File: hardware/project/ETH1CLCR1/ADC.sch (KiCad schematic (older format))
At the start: 89 parts, among them Q1101 BC847W, Q1102 BC847W, Q1103 BC847W, Q1104 BC847W, U1101 ADG419BR, U1102 ADG419BR, U1103 REF192, U1104 AD8606-2-MSOP, U1105 AD8606-2-MSOP, U1106 AD7380, U1107 AD8605, U1108 LT6350, U1109 LT6350, U1110 OPA602, U1111 OPA602, U1112 PGA103, U1113 PGA103

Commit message: PCB layout
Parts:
- U1106: symbol ETH1CLCR1:AD7380 -> ETH1CLCR1-rescue:AD7380-ETH1CLCR1
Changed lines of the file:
@@
 Connection ~ 3850 6900
 $Comp
-L ETH1CLCR1:AD7380 U1106
+L ETH1CLCR1-rescue:AD7380-ETH1CLCR1 U1106
 U 1 1 5E5D364C
 P 3450 3650
+AR Path="/5E5D364C" Ref="U1106"  Part="1"
+AR Path="/5E402F62/5E5D364C" Ref="U1106"  Part="1"
 F 0 "U1106" H 3850 4400 50  0000 C CNN
 F 1 "AD7380" H 3850 4300 50  0000 C CNN

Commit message: PCB layout
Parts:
- added C1115, C1117, C1119, C1123, C1125, C1127, C1129, C1131: 100n, Capacitor_SMD:C_0603_1608Metric_Pad1.05x0.95mm_HandSolder, symbol Device:C
- renumbered C1115 to C1116, C1116 to C1118, C1117 to C1120, C1118 to C1121, C1119 to C1122, C1120 to C1124, C1121 to C1126, C1122 to C1128, C1123 to C1130, C1124 to C1132, C1125 to C1133, C1126 to C1134, C1127 to C1135, C1128 to C1136, C1129 to C1137, C1130 to C1138, R1141 to R1139, R1142 to R1140, R1139 to R1141, R1140 to R1142
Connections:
- net +15VF: now also C1115.1, C1119.1, C1125.1, C1129.1
- net -15VF: now also C1117.1, C1123.1, C1127.1, C1131.1
- net AGNDF: now also C1115.2, C1117.2, C1119.2, C1123.2, C1125.2, C1127.2, C1129.2, C1131.2

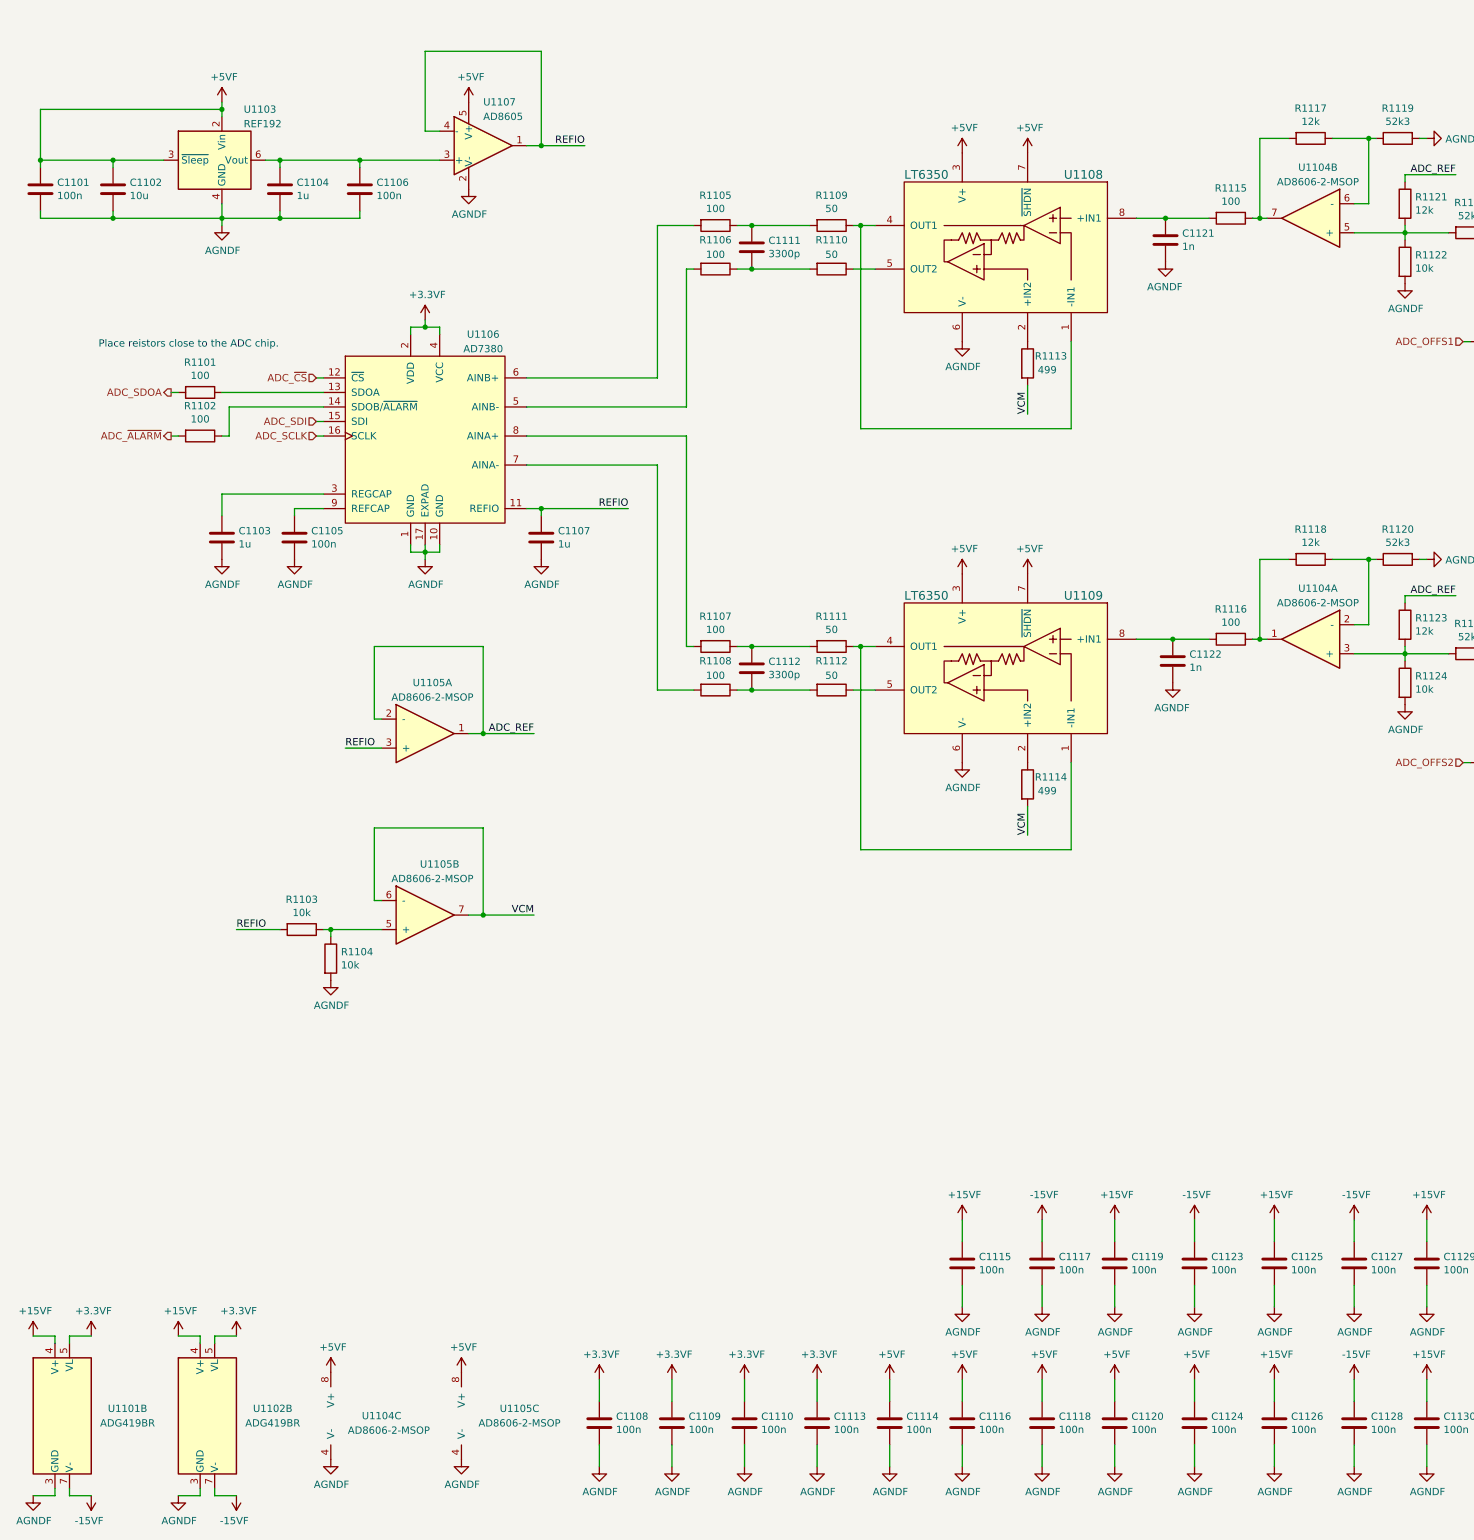
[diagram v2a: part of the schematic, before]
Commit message: Changed op-amps in ADC schematic.
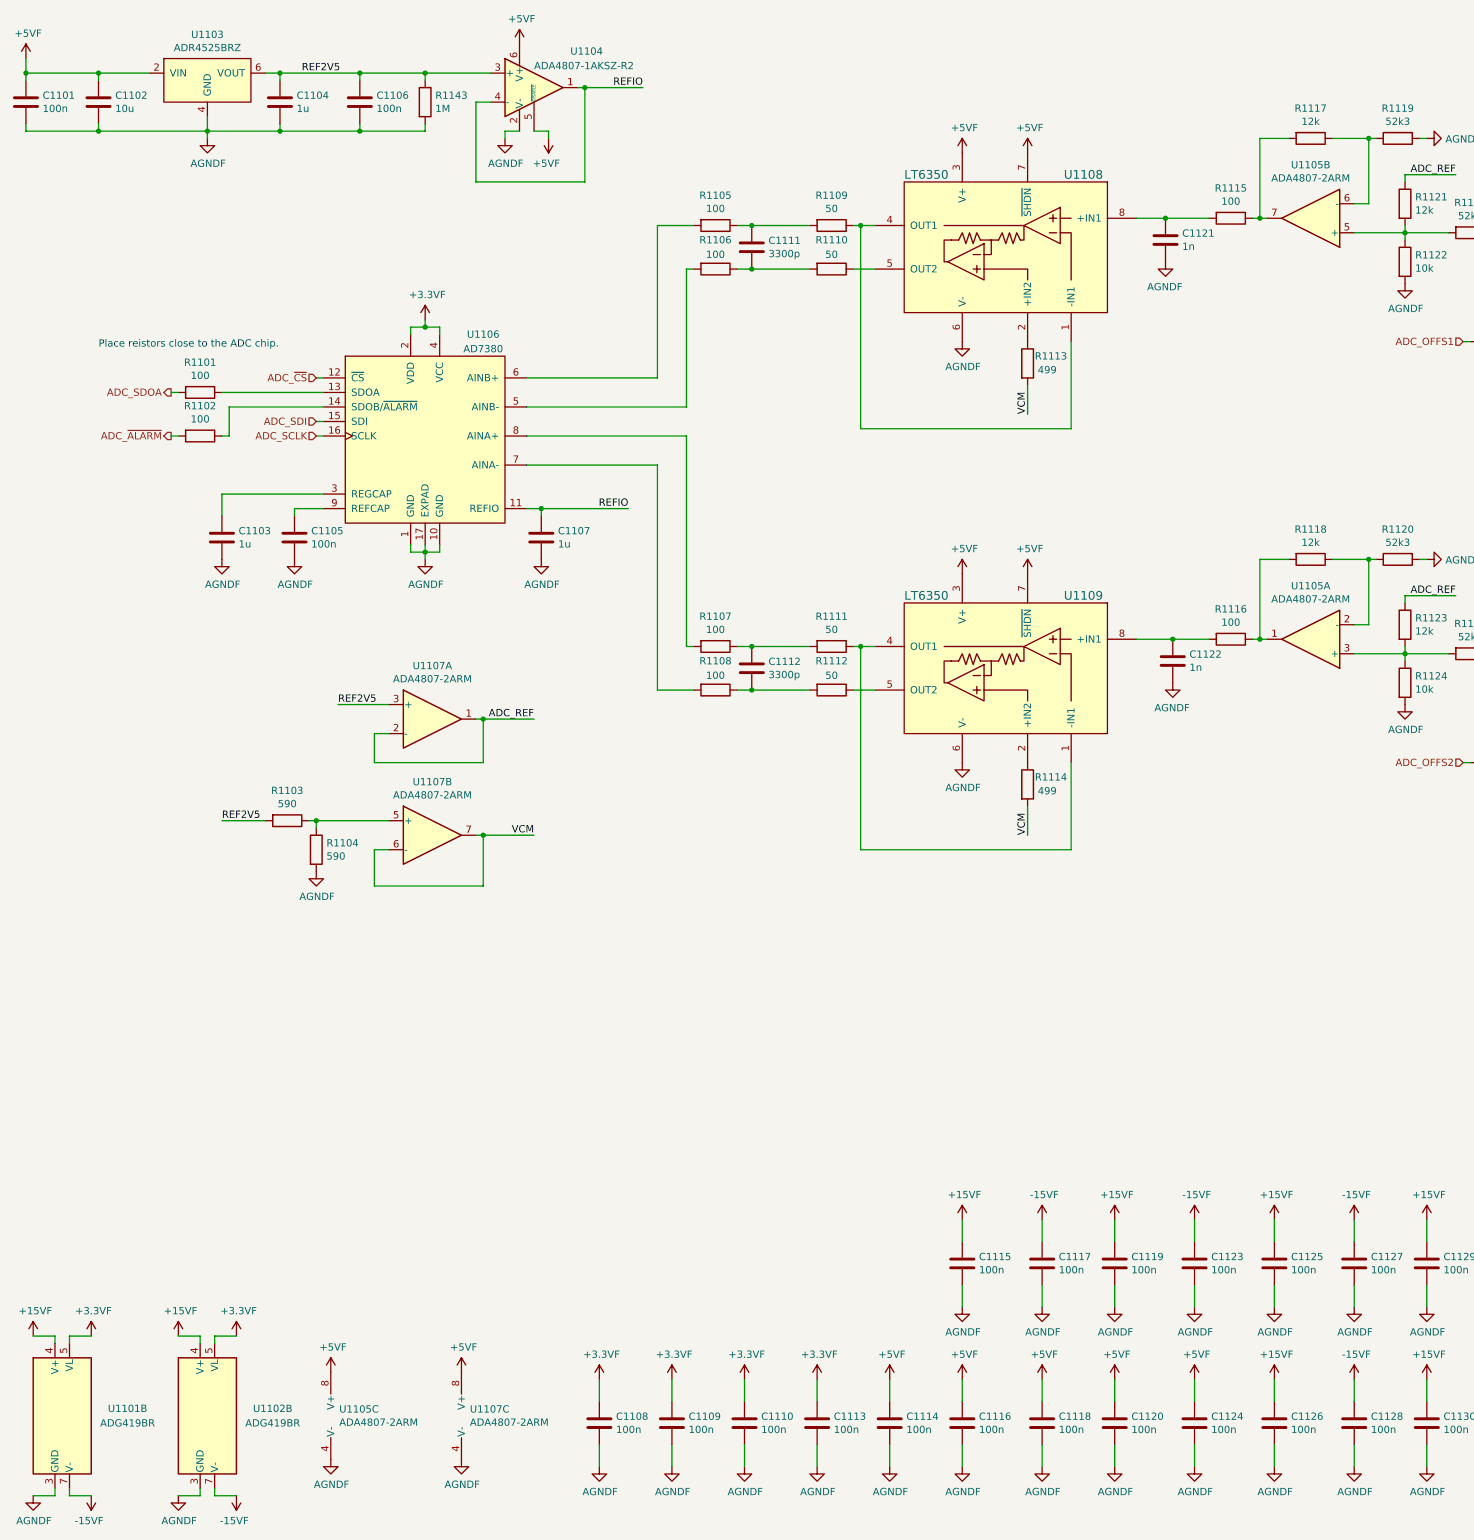
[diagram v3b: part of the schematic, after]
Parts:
- removed U1103: REF192, Package_SO:SSOP-8_3.9x5.05mm_P1.27mm, symbol Reference_Voltage:REF192
- removed U1104, U1105: AD8606-2-MSOP, Package_SO:MSOP-8_3x3mm_P0.65mm, symbol ETH1CLCR1:AD8606-2-MSOP
- removed U1107: AD8605, Package_TO_SOT_SMD:SOT-23-5_HandSoldering, symbol ETH1CLCR1:AD8605
- added R1143: 1M, Resistor_SMD:R_0603_1608Metric_Pad1.05x0.95mm_HandSolder, symbol Device:R
- added U1103: ADR4525BRZ, Package_SO:SOIC-8_3.9x4.9mm_P1.27mm, symbol ETH1CLCR1:ADR4525BRZ
- added U1104: ADA4807-1AKSZ-R2, Package_TO_SOT_SMD:SOT-363_SC-70-6_Handsoldering, symbol Amplifier_Operational:ADA4807-1
- added U1105, U1107: ADA4807-2ARM, Package_SO:MSOP-8_3x3mm_P0.65mm, symbol Amplifier_Operational:ADA4807-2ARM
- R1103, R1104: value 10k -> 590
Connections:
- net +5VF: now also U1103.2 (VIN), U1104.5 (~DISABLE), U1104.6 (V+), U1105.8 (V+), U1107.8 (V+)
- net ADC_REF: now also U1107.1, U1107.2 (-)
- net AGNDF: now also R1143.2, U1103.4 (GND), U1104.2 (V-), U1105.4 (V-), U1107.4 (V-)
- net REFIO: now also U1104.1, U1104.4 (-); no longer R1103.2
- net VCM: now also U1107.6 (-), U1107.7
- net at R1115.1, R1117.2: now also U1105.7
- net at R1103.1, R1104.1: now also U1107.5 (+)
- net at R1121.2, R1122.1, R1125.2: now also U1105.5 (+)
- net at R1117.1, R1119.1: now also U1105.6 (-)
- net at R1116.1, R1118.2: now also U1105.1
- net at R1123.2, R1124.1, R1126.2: now also U1105.3 (+)
- net at R1118.1, R1120.1: now also U1105.2 (-)
- net REF2V5: now reaches C1104.1, C1106.1
- net REF2V5: now also R1103.2, R1143.1, U1103.6 (VOUT), U1104.3 (+), U1107.3 (+)
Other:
- moved on the sheet: C1101, C1102, C1104, C1106, R1103, R1104

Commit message: PCB layout
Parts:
- added C1139, C1140: 100n, Capacitor_SMD:C_0603_1608Metric_Pad1.05x0.95mm_HandSolder, symbol Device:C
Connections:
- net AGNDF: now also C1139.2, C1140.2
- net at R1113.1, U1108.2 (+IN2): now also C1139.1
- net at R1114.1, U1109.2 (+IN2): now also C1140.1
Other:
- moved on the sheet: R1113, R1114
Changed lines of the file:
@@
 	1    0    0    -1
 $EndComp
-Text Label 7600 3450 1    50   ~ 0
+Text Label 7600 3800 1    50   ~ 0
 VCM
 Wire Wire Line
-	7600 3450 7600 3250
-Wire Wire Line
-	6450 5050 6550 5050
-Wire Wire Line
-	7900 2950 7900 3550
-Wire Wire Line
-	7900 3550 6450 3550
-Wire Wire Line
-	6450 3550 6450 2150
+	7600 3800 7600 3600
+Wire Wire Line
+	7900 2950 7900 3900
+Wire Wire Line
+	7900 3900 6450 3900
+Wire Wire Line
+	6450 3900 6450 2150
 Wire Wire Line
 	6550 2150 6450 2150
@@
 	6400 5350 6550 5350
 Wire Wire Line
-	6450 5050 6400 5050
-Wire Wire Line
 	6100 5050 5700 5050
 Wire Wire Line
@@
 	5600 5350 5700 5350
 Connection ~ 5700 5350
-Connection ~ 6450 5050
 Wire Wire Line
 	5300 5050 5250 5050
@@
 L Device:R R1113
 U 1 1 5E246E09
-P 7600 3100
-F 0 "R1113" H 7650 3150 50  0000 L CNN
-F 1 "499" H 7670 3055 50  0000 L CNN
-F 2 "Resistor_SMD:R_0603_1608Metric_Pad1.05x0.95mm_HandSolder" V 7530 3100 50  0001 C CNN
-F 3 "~" H 7600 3100 50  0001 C CNN
-	1    7600 3100
-	1    0    0    -1
-$EndComp
-Wire Wire Line
-	7900 5850 7900 6450
-Wire Wire Line
-	7900 6450 6450 6450
-Wire Wire Line
-	6450 5050 6450 6450
-Text Label 7600 6350 1    50   ~ 0
+P 7600 3450
+F 0 "R1113" H 7650 3500 50  0000 L CNN
+F 1 "499" H 7670 3405 50  0000 L CNN
+F 2 "Resistor_SMD:R_0603_1608Metric_Pad1.05x0.95mm_HandSolder" V 7530 3450 50  0001 C CNN
+F 3 "~" H 7600 3450 50  0001 C CNN
+	1    7600 3450
+	1    0    0    -1
+$EndComp
+Text Label 7600 6700 1    50   ~ 0
 VCM
 Wire Wire Line
-	7600 6350 7600 6150
+	7600 6700 7600 6500
 $Comp
 L Device:R R1114
 U 1 1 5E310DDA
-P 7600 6000
-F 0 "R1114" H 7650 6050 50  0000 L CNN
-F 1 "499" H 7670 5955 50  0000 L CNN
-F 2 "Resistor_SMD:R_0603_1608Metric_Pad1.05x0.95mm_HandSolder" V 7530 6000 50  0001 C CNN
-F 3 "~" H 7600 6000 50  0001 C CNN
-	1    7600 6000
+P 7600 6350
+F 0 "R1114" H 7650 6400 50  0000 L CNN
+F 1 "499" H 7670 6305 50  0000 L CNN
+F 2 "Resistor_SMD:R_0603_1608Metric_Pad1.05x0.95mm_HandSolder" V 7530 6350 50  0001 C CNN
+F 3 "~" H 7600 6350 50  0001 C CNN
+	1    7600 6350
 	1    0    0    -1
 $EndComp
@@
 	1    0    0    -1
 $EndComp
+$Comp
+L Device:C C1139
+U 1 1 5E3B70FC
+P 7200 3450
+F 0 "C1139" H 7315 3496 50  0000 L CNN
+F 1 "100n" H 7315 3405 50  0000 L CNN
+F 2 "Capacitor_SMD:C_0603_1608Metric_Pad1.05x0.95mm_HandSolder" H 7238 3300 50  0001 C CNN
+F 3 "~" H 7200 3450 50  0001 C CNN
+	1    7200 3450
+	1    0    0    -1
+$EndComp
+$Comp
+L ETH1CLCR1:AGNDF #PWR0106
+U 1 1 5E3B7653
+P 7200 3600
+F 0 "#PWR0106" H 7200 3350 50  0001 C CNN
+F 1 "AGNDF" H 7205 3427 50  0000 C CNN
+F 2 "" H 7200 3600 50  0001 C CNN
+F 3 "" H 7200 3600 50  0001 C CNN
+	1    7200 3600
+	1    0    0    -1
+$EndComp
+Wire Wire Line
+	7200 3300 7200 3250
+Wire Wire Line
+	7200 3250 7600 3250
+Wire Wire Line
+	7600 3250 7600 3300
+Wire Wire Line
+	7600 3250 7600 2950
+Connection ~ 7600 3250
+Wire Wire Line
+	6400 5050 6450 5050
+Wire Wire Line
+	7900 5850 7900 6800
+Wire Wire Line
+	7900 6800 6450 6800
+Wire Wire Line
+	6450 6800 6450 5050
+Wire Wire Line
+	7600 6150 7600 5850
+$Comp
+L Device:C C1140
+U 1 1 5E48656C
+P 7200 6350
+F 0 "C1140" H 7315 6396 50  0000 L CNN
+F 1 "100n" H 7315 6305 50  0000 L CNN
+F 2 "Capacitor_SMD:C_0603_1608Metric_Pad1.05x0.95mm_HandSolder" H 7238 6200 50  0001 C CNN
+F 3 "~" H 7200 6350 50  0001 C CNN
+	1    7200 6350
+	1    0    0    -1
+$EndComp
+$Comp
+L ETH1CLCR1:AGNDF #PWR0107
+U 1 1 5E486572
+P 7200 6500
+F 0 "#PWR0107" H 7200 6250 50  0001 C CNN
+F 1 "AGNDF" H 7205 6327 50  0000 C CNN
+F 2 "" H 7200 6500 50  0001 C CNN
+F 3 "" H 7200 6500 50  0001 C CNN
+	1    7200 6500
+	1    0    0    -1
+$EndComp
+Wire Wire Line
+	7200 6200 7200 6150
+Wire Wire Line
+	7200 6150 7600 6150
+Wire Wire Line
+	7600 6200 7600 6150
+Connection ~ 7600 6150
+Connection ~ 6450 5050
+Wire Wire Line
+	6450 5050 6550 5050
 $EndSCHEMATC

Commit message: PCB layout
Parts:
- added R1101, R1104, R1105: 0, Resistor_SMD:R_0603_1608Metric_Pad1.05x0.95mm_HandSolder, symbol Device:R
- renumbered C1139 to C1117, C1140 to C1118, C1117 to C1119, C1118 to C1120, C1119 to C1121, C1120 to C1122, C1121 to C1123, C1122 to C1124, C1123 to C1125, C1124 to C1126, C1125 to C1127, C1126 to C1128, C1127 to C1129, C1128 to C1130, C1129 to C1131, C1130 to C1132, C1131 to C1133, C1132 to C1134, C1133 to C1135, C1134 to C1136, C1135 to C1137, C1136 to C1138, C1137 to C1139, C1138 to C1140, R1101 to R1102, R1102 to R1103, R1103 to R1106, R1104 to R1107, R1143 to R1108, R1105 to R1109, R1106 to R1110, R1107 to R1111, R1108 to R1112, R1109 to R1113, R1110 to R1114, R1111 to R1115, R1112 to R1116, R1113 to R1117, R1114 to R1118, R1115 to R1119, R1116 to R1120, R1117 to R1121, R1118 to R1122, R1119 to R1123, R1120 to R1124, R1121 to R1125, R1122 to R1126, R1123 to R1127, R1124 to R1128, R1125 to R1129, R1126 to R1130, R1127 to R1131, R1128 to R1132, R1129 to R1133, R1130 to R1134, R1131 to R1135, R1132 to R1136, R1133 to R1137, R1134 to R1138, R1135 to R1139, R1136 to R1140, R1137 to R1141, R1138 to R1142, R1139 to R1143, R1140 to R1144, R1141 to R1145, R1142 to R1146, U1105 to U1104, U1107 to U1106, U1104 to U1107
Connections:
- net ADC_SCLK: now also R1105.2; no longer U1106.16 (SCLK)
- net ADC_SDI: now also R1104.2; no longer U1106.15 (SDI)
- net ADC_~CS: now also R1101.2; no longer U1106.12 (~CS)
- new net: R1101.1, U1106.12 (~CS)
- new net: R1104.1, U1106.15 (SDI)
- new net: R1105.1, U1106.16 (SCLK)
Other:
- moved on the sheet: R1102, R1103

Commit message: PCB done.
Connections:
- net VCM renamed CMV
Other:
- moved on the sheet: C1117, C1118
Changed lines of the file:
@@
 $EndComp
 Text Label 7600 3800 1    50   ~ 0
-VCM
+CMV
 Wire Wire Line
 	7600 3800 7600 3600
@@
 $EndComp
 Text Label 7600 6700 1    50   ~ 0
-VCM
+CMV
 Wire Wire Line
 	7600 6700 7600 6500
@@
 	2650 6250 2700 6250
 Text Label 4200 6350 2    50   ~ 0
-VCM
+CMV
 $Comp
 L Amplifier_Operational:ADA4807-2ARM U1106
@@
 L Device:C C1117
 U 1 1 5E3B70FC
-P 7200 3450
-F 0 "C1117" H 7315 3496 50  0000 L CNN
-F 1 "100n" H 7315 3405 50  0000 L CNN
-F 2 "Capacitor_SMD:C_0603_1608Metric_Pad1.05x0.95mm_HandSolder" H 7238 3300 50  0001 C CNN
-F 3 "~" H 7200 3450 50  0001 C CNN
-	1    7200 3450
+P 7150 3450
+F 0 "C1117" H 7265 3496 50  0000 L CNN
+F 1 "100n" H 7265 3405 50  0000 L CNN
+F 2 "Capacitor_SMD:C_0603_1608Metric_Pad1.05x0.95mm_HandSolder" H 7188 3300 50  0001 C CNN
+F 3 "~" H 7150 3450 50  0001 C CNN
+	1    7150 3450
 	1    0    0    -1
 $EndComp
@@
 L ETH1CLCR1:AGNDF #PWR01142
 U 1 1 5E3B7653
-P 7200 3600
-F 0 "#PWR01142" H 7200 3350 50  0001 C CNN
-F 1 "AGNDF" H 7205 3427 50  0000 C CNN
-F 2 "" H 7200 3600 50  0001 C CNN
-F 3 "" H 7200 3600 50  0001 C CNN
-	1    7200 3600
-	1    0    0    -1
-$EndComp
-Wire Wire Line
-	7200 3300 7200 3250
-Wire Wire Line
-	7200 3250 7600 3250
+P 7150 3600
+F 0 "#PWR01142" H 7150 3350 50  0001 C CNN
+F 1 "AGNDF" H 7155 3427 50  0000 C CNN
+F 2 "" H 7150 3600 50  0001 C CNN
+F 3 "" H 7150 3600 50  0001 C CNN
+	1    7150 3600
+	1    0    0    -1
+$EndComp
+Wire Wire Line
+	7150 3300 7150 3250
+Wire Wire Line
+	7150 3250 7600 3250
 Wire Wire Line
 	7600 3250 7600 3300
@@
 Wire Wire Line
 	6450 6800 6450 5050
-Wire Wire Line
-	7600 6150 7600 5850
 $Comp
 L Device:C C1118
 U 1 1 5E48656C
-P 7200 6350
-F 0 "C1118" H 7315 6396 50  0000 L CNN
-F 1 "100n" H 7315 6305 50  0000 L CNN
-F 2 "Capacitor_SMD:C_0603_1608Metric_Pad1.05x0.95mm_HandSolder" H 7238 6200 50  0001 C CNN
-F 3 "~" H 7200 6350 50  0001 C CNN
-	1    7200 6350
+P 7150 6350
+F 0 "C1118" H 7265 6396 50  0000 L CNN
+F 1 "100n" H 7265 6305 50  0000 L CNN
+F 2 "Capacitor_SMD:C_0603_1608Metric_Pad1.05x0.95mm_HandSolder" H 7188 6200 50  0001 C CNN
+F 3 "~" H 7150 6350 50  0001 C CNN
+	1    7150 6350
 	1    0    0    -1
 $EndComp
@@
 L ETH1CLCR1:AGNDF #PWR01143
 U 1 1 5E486572
-P 7200 6500
-F 0 "#PWR01143" H 7200 6250 50  0001 C CNN
-F 1 "AGNDF" H 7205 6327 50  0000 C CNN
-F 2 "" H 7200 6500 50  0001 C CNN
-F 3 "" H 7200 6500 50  0001 C CNN
-	1    7200 6500
-	1    0    0    -1
-$EndComp
-Wire Wire Line
-	7200 6200 7200 6150
-Wire Wire Line
-	7200 6150 7600 6150
-Wire Wire Line
-	7600 6200 7600 6150
-Connection ~ 7600 6150
+P 7150 6500
+F 0 "#PWR01143" H 7150 6250 50  0001 C CNN
+F 1 "AGNDF" H 7155 6327 50  0000 C CNN
+F 2 "" H 7150 6500 50  0001 C CNN
+F 3 "" H 7150 6500 50  0001 C CNN
+	1    7150 6500
+	1    0    0    -1
+$EndComp
+Wire Wire Line
+	7150 6200 7150 6150
 Connection ~ 6450 5050
 Wire Wire Line
@@
 Wire Wire Line
 	1950 3800 2000 3800
+Wire Wire Line
+	7600 5850 7600 6150
+Wire Wire Line
+	7150 6150 7600 6150
+Connection ~ 7600 6150
+Wire Wire Line
+	7600 6150 7600 6200
 $EndSCHEMATC
